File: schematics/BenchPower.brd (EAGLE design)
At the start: 79.7 x 67 mm, 28 parts, among them U1 V_REG_317SINK

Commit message: New layout
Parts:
- moved JP7 50.8 mm to (8.89, 6.99), turned to 90 degrees
- moved U$3 49.8 mm to (1.91, 58.7)
- moved JP2 46.4 mm to (51.4, 3.81), turned to 0 degrees
- moved JP6 26.7 mm to (31.8, 3.81), turned to 0 degrees
- moved R1 6.87 mm to (31.8, 31.8)
- moved LED1 3.18 mm to (33.0, 10.2)
- moved PWR1 3.18 mm to (62.9, 6.35)
- moved PWR2 3.18 mm to (23.5, 6.35)
- moved U$5 3.17 mm to (43.2, 6.35)
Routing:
- net 5VATX: track 55.1 -> 99.9 mm
- net AMPS12VHDR: track 68.8 -> 61.0 mm
- net 12VHDR: track 103.8 -> 96.6 mm
- net N$1: track 15.0 -> 17.8 mm
- net AMPS12VREG: track 66.1 -> 63.5 mm
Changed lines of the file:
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@@
 <wire x1="79.6825" y1="67" x2="0" y2="67" width="0" layer="20"/>
 <wire x1="0" y1="67" x2="0" y2="0" width="0" layer="20"/>
-<text x="1.27" y="10.795" size="1.27" layer="21" font="vector">cjd@chrisd.info</text>
-<text x="65.0875" y="10.795" size="1.27" layer="21" font="vector">v2.0 (c) 2015</text>
-<text x="64.135" y="1.27" size="1.27" layer="21" font="vector">adj</text>
-<text x="24.765" y="1.27" size="1.27" layer="21" font="vector">12v</text>
-<text x="43.18" y="12.7" size="1.27" layer="21" font="vector">blog.chrisd.info</text>
-<text x="45.085" y="1.27" size="1.27" layer="21" font="vector">gnd</text>
-<text x="6.985" y="4.445" size="1.27" layer="21" font="vector">12v</text>
-<text x="6.985" y="1.905" size="1.27" layer="21" font="vector">gnd</text>
+<text x="1.905" y="53.975" size="1.27" layer="21" font="vector">cjd@chrisd.info</text>
+<text x="1.905" y="56.515" size="1.27" layer="21" font="vector">v2.0 (c) 2015</text>
+<text x="27.94" y="1.27" size="1.27" layer="21" font="vector">12v</text>
+<text x="1.905" y="51.435" size="1.27" layer="21" font="vector">blog.chrisd.info</text>
+<text x="48.26" y="1.27" size="1.27" layer="21" font="vector">gnd</text>
 <text x="73.025" y="5.715" size="1.27" layer="21" font="vector" rot="R180">adj</text>
 <text x="73.025" y="3.175" size="1.27" layer="21" font="vector" rot="R180">gnd</text>
@@
 </autorouter>
 <elements>
-<element name="PWR1" library="desjardins" package="BINDINGPOST" value="BINDINGPOST" x="59.69" y="6.35"/>
-<element name="PWR2" library="desjardins" package="BINDINGPOST" value="BINDINGPOST" x="20.32" y="6.35"/>
-<element name="U$5" library="desjardins" package="BINDINGPOST" value="BINDINGPOST" x="40.005" y="6.35"/>
+<element name="PWR1" library="desjardins" package="BINDINGPOST" value="BINDINGPOST" x="62.865" y="6.35"/>
+<element name="PWR2" library="desjardins" package="BINDINGPOST" value="BINDINGPOST" x="23.495" y="6.35"/>
+<element name="U$5" library="desjardins" package="BINDINGPOST" value="BINDINGPOST" x="43.18" y="6.35"/>
 <element name="ATXCONN" library="desjardins" package="ATXPOWER" value="ATXPOWER" x="48.26" y="55.88" rot="R270"/>
 <element name="ARDUINOMICRO" library="ChrisD" package="ARDUINO_PRO_MICRO" value="ARDUINO_PRO_MICRO" x="78.105" y="22.225" rot="R90"/>
 <element name="U1" library="SparkFun-PowerIC" package="TO220-ADJ" value="V_REG_317SINK" x="77.47" y="61.595" rot="R270"/>
-<element name="R1" library="SparkFun-Passives" package="AXIAL-0.3" value="1000" x="26.035" y="27.94" rot="R270"/>
+<element name="R1" library="SparkFun-Passives" package="AXIAL-0.3" value="1000" x="31.75" y="31.75" rot="R270"/>
 <element name="R2" library="SparkFun-Passives" package="AXIAL-0.3" value="240" x="73.025" y="60.325" rot="R270"/>
-<element name="U$3" library="desjardins" package="LOGO" value="" x="21.59" y="13.0175"/>
+<element name="U$3" library="desjardins" package="LOGO" value="" x="1.905" y="58.7375"/>
 <element name="LCD" library="desjardins" package="DT162C" value="16X2LCDDT162C" x="40.01" y="31.135"/>
-<element name="LED1" library="adafruit" package="LED3MM" value="" x="29.845" y="10.16"/>
+<element name="LED1" library="adafruit" package="LED3MM" value="" x="33.02" y="10.16"/>
 <element name="R6" library="SparkFun-Resistors" package="1206" value="" x="48.895" y="32.385" rot="R180"/>
 <element name="R7" library="SparkFun-Resistors" package="1206" value="" x="65.405" y="32.385" rot="R180"/>
@@
 <element name="R8" library="SparkFun-Passives" package="AXIAL-0.3" value="gain" x="52.705" y="31.115" rot="R270"/>
 <element name="R9" library="SparkFun-Passives" package="AXIAL-0.3" value="gain" x="69.215" y="31.115" rot="R270"/>
-<element name="JP2" library="SparkFun-Connectors" package="1X02" value="M02PTH" x="5.08" y="2.54" rot="R180"/>
+<element name="JP2" library="SparkFun-Connectors" package="1X02" value="M02PTH" x="51.435" y="3.81"/>
 <element name="R3" library="SparkFun-Passives" package="AXIAL-0.3" value="100" x="55.245" y="31.115" rot="R90"/>
 <element name="R10" library="SparkFun-Passives" package="AXIAL-0.3" value="140" x="57.785" y="31.115" rot="R90"/>
 <element name="JP4" library="SparkFun-Connectors" package="1X02" value="M02PTH" x="74.93" y="2.54"/>
 <element name="JP5" library="SparkFun-Connectors" package="1X02" value="M02PTH" x="74.93" y="5.08"/>
-<element name="JP6" library="SparkFun-Connectors" package="1X02" value="M02PTH" x="5.08" y="5.08" rot="R180"/>
-<element name="JP7" library="SparkFun-Connectors" package="USB-A-S" value="USB-A-S" x="9.525" y="57.785"/>
+<element name="JP6" library="SparkFun-Connectors" package="1X02" value="M02PTH" x="31.75" y="3.81"/>
+<element name="JP7" library="SparkFun-Connectors" package="USB-A-S" value="USB-A-S" x="8.89" y="6.985" rot="R90"/>
 <element name="JP8" library="SparkFun-Connectors" package="1X03" value="" x="62.23" y="44.45"/>
 </elements>
@@
 <wire x1="40.005" y1="36.83" x2="57.785" y2="36.83" width="0.8128" layer="1"/>
 <wire x1="57.785" y1="36.83" x2="57.785" y2="34.925" width="0.8128" layer="1"/>
-<wire x1="31.115" y1="36.83" x2="36.83" y2="36.83" width="0.4064" layer="1"/>
-<wire x1="36.83" y1="36.83" x2="38.735" y2="38.735" width="0.4064" layer="1"/>
-<wire x1="31.115" y1="36.83" x2="26.035" y2="31.75" width="0.4064" layer="1"/>
+<wire x1="31.75" y1="35.56" x2="35.56" y2="35.56" width="0.4064" layer="1"/>
+<wire x1="35.56" y1="35.56" x2="38.735" y2="38.735" width="0.4064" layer="1"/>
 </signal>
 <signal name="N$1">
 <contactref element="R1" pad="P$2"/>
 <contactref element="LED1" pad="A"/>
-<wire x1="26.035" y1="24.13" x2="26.035" y2="12.7" width="0.4064" layer="16"/>
-<wire x1="26.035" y1="12.7" x2="28.575" y2="10.16" width="0.4064" layer="16"/>
+<wire x1="31.75" y1="27.94" x2="31.75" y2="10.16" width="0.4064" layer="1"/>
 </signal>
 <signal name="PWR_OK">
@@
 <wire x1="60.96" y1="26.67" x2="62.23" y2="25.4" width="0.8128" layer="1"/>
 <wire x1="62.23" y1="25.4" x2="74.93" y2="25.4" width="0.8128" layer="1"/>
-<wire x1="76.2" y1="22.225" x2="74.93" y2="20.955" width="0.8128" layer="1"/>
+<wire x1="76.2" y1="22.225" x2="74.295" y2="20.32" width="0.8128" layer="1"/>
 <wire x1="74.93" y1="5.08" x2="77.47" y2="5.08" width="0.8128" layer="16"/>
-<wire x1="74.93" y1="20.955" x2="74.93" y2="13.335" width="0.8128" layer="1"/>
-<wire x1="74.93" y1="13.335" x2="77.47" y2="10.795" width="0.8128" layer="1"/>
+<wire x1="74.295" y1="20.32" x2="74.295" y2="13.97" width="0.8128" layer="1"/>
+<wire x1="74.295" y1="13.97" x2="77.47" y2="10.795" width="0.8128" layer="1"/>
 <wire x1="77.47" y1="10.795" x2="77.47" y2="5.08" width="0.8128" layer="1"/>
-<wire x1="74.93" y1="5.08" x2="60.96" y2="5.08" width="0.8128" layer="16"/>
-<wire x1="60.96" y1="5.08" x2="59.69" y2="6.35" width="0.8128" layer="16"/>
+<wire x1="74.93" y1="5.08" x2="64.135" y2="5.08" width="0.8128" layer="16"/>
+<wire x1="64.135" y1="5.08" x2="62.865" y2="6.35" width="0.8128" layer="16"/>
 </signal>
 <signal name="AMPS12VHDR">
@@
 <wire x1="47.5949" y1="29.525" x2="47.5949" y2="31.6501" width="0.4064" layer="1"/>
 <wire x1="47.5949" y1="31.6501" x2="47.495" y2="32.385" width="0.6096" layer="1"/>
-<wire x1="20.32" y1="22.86" x2="20.32" y2="6.35" width="0.8128" layer="1"/>
-<wire x1="20.32" y1="22.86" x2="29.845" y2="32.385" width="0.8128" layer="1"/>
 <wire x1="29.845" y1="32.385" x2="47.495" y2="32.385" width="0.8128" layer="1"/>
 <contactref element="JP6" pad="2"/>
 <contactref element="JP6" pad="1"/>
-<wire x1="2.54" y1="5.08" x2="5.08" y2="5.08" width="0.8128" layer="16"/>
-<wire x1="5.08" y1="5.08" x2="19.05" y2="5.08" width="0.8128" layer="16"/>
-<wire x1="19.05" y1="5.08" x2="20.32" y2="6.35" width="0.8128" layer="16"/>
+<wire x1="29.845" y1="32.385" x2="23.495" y2="26.035" width="0.8128" layer="1"/>
+<wire x1="23.495" y1="26.035" x2="23.495" y2="6.35" width="0.8128" layer="1"/>
+<wire x1="23.495" y1="6.35" x2="29.21" y2="6.35" width="0.8128" layer="1"/>
+<wire x1="29.21" y1="6.35" x2="31.75" y2="3.81" width="0.8128" layer="1"/>
+<wire x1="31.75" y1="3.81" x2="34.29" y2="3.81" width="0.8128" layer="1"/>
 </signal>
 <signal name="3.3V$2">
@@
 <contactref element="LCD" pad="P$4"/>
 <contactref element="ARDUINOMICRO" pad="P3"/>
-<wire x1="35.56" y1="26.67" x2="38.735" y2="23.495" width="0.4064" layer="16"/>
-<wire x1="35.56" y1="26.67" x2="34.925" y2="26.67" width="0.4064" layer="16"/>
-<wire x1="34.925" y1="26.67" x2="15.875" y2="45.72" width="0.4064" layer="16"/>
-<wire x1="15.875" y1="45.72" x2="15.875" y2="46.89" width="0.4064" layer="16"/>
-<wire x1="15.875" y1="46.89" x2="15.63" y2="47.135" width="0.4064" layer="16"/>
+<wire x1="38.735" y1="23.495" x2="15.63" y2="46.6" width="0.4064" layer="16"/>
+<wire x1="15.63" y1="46.6" x2="15.63" y2="47.135" width="0.4064" layer="16"/>
 </signal>
 <signal name="LCD_EN">
@@
 <wire x1="62.865" y1="51.435" x2="62.865" y2="50.475" width="0.4064" layer="1"/>
 <wire x1="62.865" y1="50.475" x2="62.96" y2="50.38" width="0.4064" layer="1"/>
-<wire x1="60.96" y1="53.34" x2="22.86" y2="53.34" width="0.4064" layer="1"/>
-<wire x1="22.86" y1="53.34" x2="15.24" y2="60.96" width="0.4064" layer="1"/>
-<wire x1="15.24" y1="60.96" x2="13.15" y2="60.96" width="0.4064" layer="1"/>
-<wire x1="13.15" y1="60.96" x2="12.975" y2="60.785" width="0.4064" layer="1"/>
+<wire x1="60.96" y1="53.34" x2="9.525" y2="53.34" width="0.4064" layer="1"/>
+<wire x1="9.525" y1="53.34" x2="5.715" y2="49.53" width="0.4064" layer="1"/>
+<wire x1="5.715" y1="49.53" x2="5.715" y2="10.61" width="0.4064" layer="1"/>
+<wire x1="5.715" y1="10.61" x2="5.89" y2="10.435" width="0.4064" layer="1"/>
 </signal>
 <signal name="5V$4">

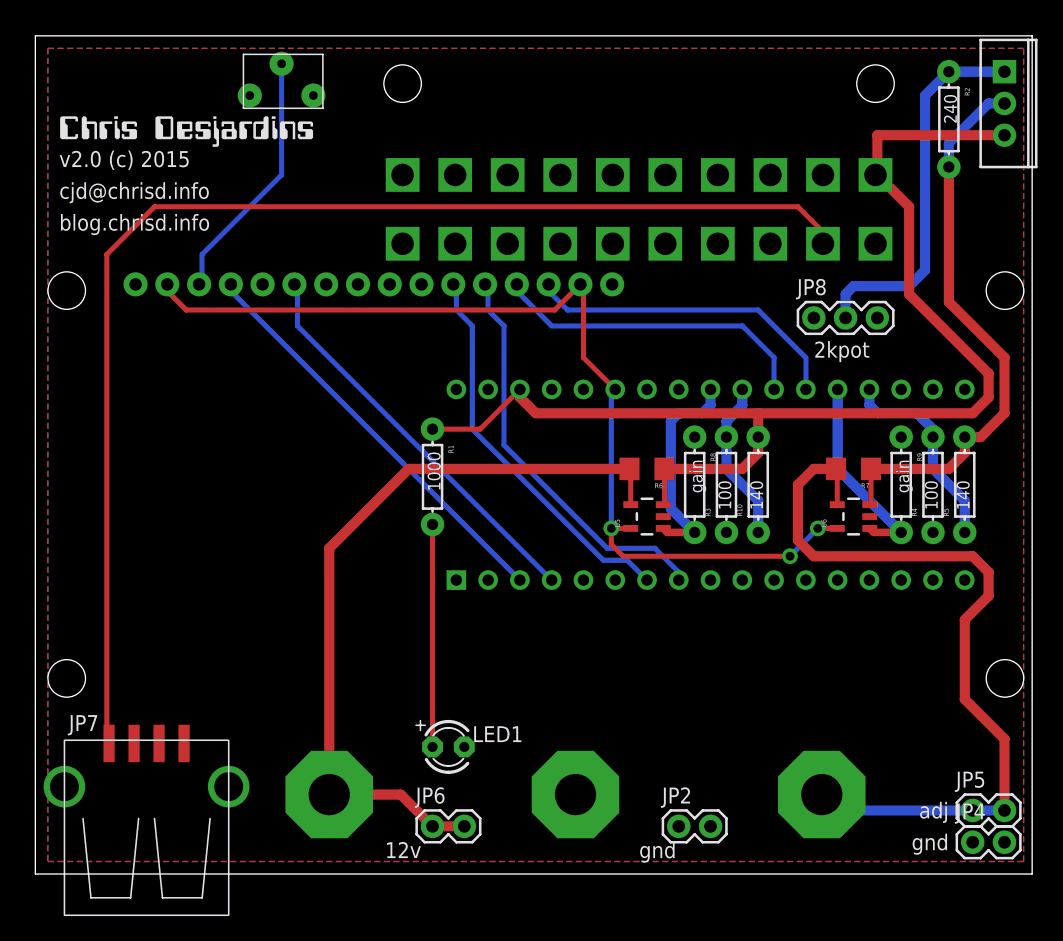
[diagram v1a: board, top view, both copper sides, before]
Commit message: Rearrange graphics
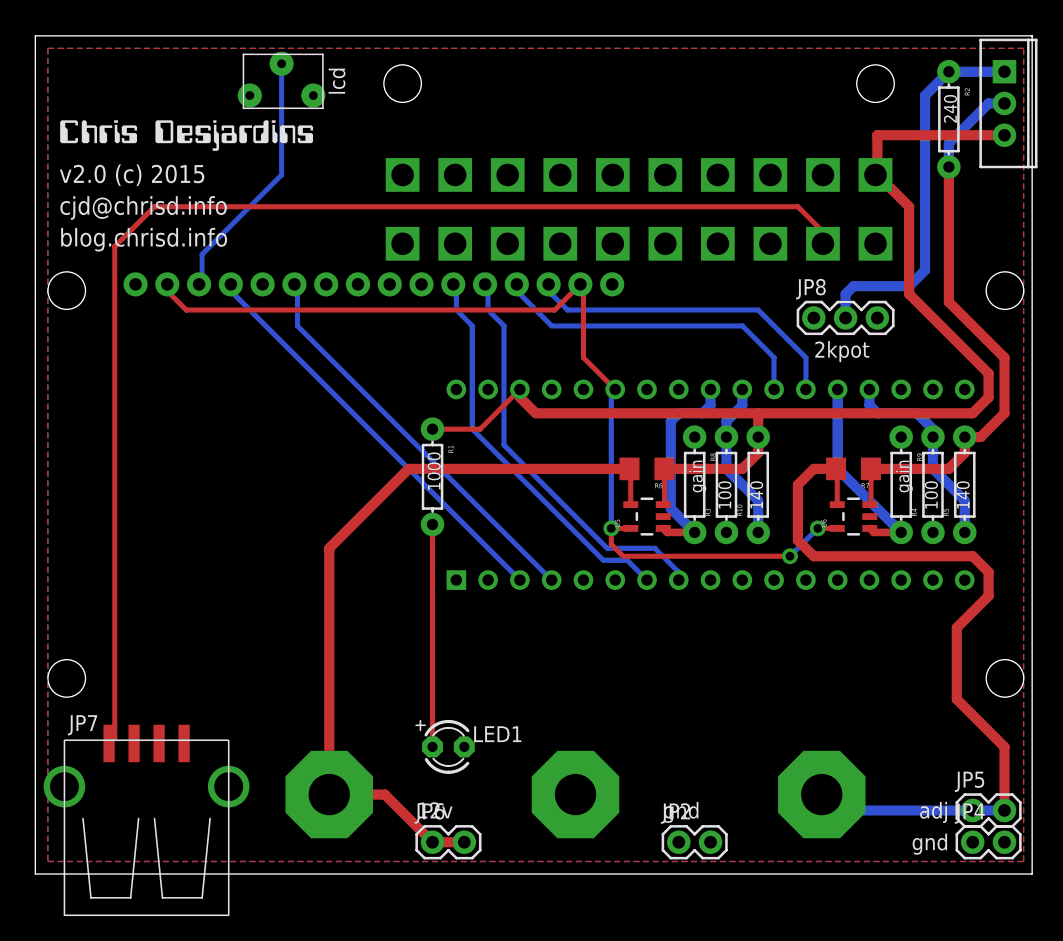
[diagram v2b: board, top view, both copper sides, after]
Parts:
- moved JP2 1.27 mm to (51.4, 2.54)
- moved JP6 1.27 mm to (31.8, 2.54)
- moved U$3 0.32 mm to (1.91, 58.4)
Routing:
- net AMPS12VHDR: track 61.0 -> 61.6 mm
- net AMPS12VREG: track 63.5 -> 64.0 mm
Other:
- board text added: "lcd"
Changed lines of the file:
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@@
 <wire x1="79.6825" y1="67" x2="0" y2="67" width="0" layer="20"/>
 <wire x1="0" y1="67" x2="0" y2="0" width="0" layer="20"/>
-<text x="1.905" y="53.975" size="1.27" layer="21" font="vector">cjd@chrisd.info</text>
-<text x="1.905" y="56.515" size="1.27" layer="21" font="vector">v2.0 (c) 2015</text>
-<text x="27.94" y="1.27" size="1.27" layer="21" font="vector">12v</text>
-<text x="1.905" y="51.435" size="1.27" layer="21" font="vector">blog.chrisd.info</text>
-<text x="48.26" y="1.27" size="1.27" layer="21" font="vector">gnd</text>
+<text x="1.905" y="52.705" size="1.4224" layer="21" font="vector">cjd@chrisd.info</text>
+<text x="1.905" y="55.245" size="1.4224" layer="21" font="vector">v2.0 (c) 2015</text>
+<text x="30.48" y="4.445" size="1.27" layer="21" font="vector">12v</text>
+<text x="1.905" y="50.165" size="1.4224" layer="21" font="vector">blog.chrisd.info</text>
+<text x="50.165" y="4.445" size="1.27" layer="21" font="vector">gnd</text>
 <text x="73.025" y="5.715" size="1.27" layer="21" font="vector" rot="R180">adj</text>
 <text x="73.025" y="3.175" size="1.27" layer="21" font="vector" rot="R180">gnd</text>
 <text x="62.23" y="41.275" size="1.27" layer="21" font="vector">2kpot</text>
+<text x="24.765" y="62.23" size="1.27" layer="21" font="vector" rot="R90">lcd</text>
 </plain>
 <attributes>
@@
 <element name="R1" library="SparkFun-Passives" package="AXIAL-0.3" value="1000" x="31.75" y="31.75" rot="R270"/>
 <element name="R2" library="SparkFun-Passives" package="AXIAL-0.3" value="240" x="73.025" y="60.325" rot="R270"/>
-<element name="U$3" library="desjardins" package="LOGO" value="" x="1.905" y="58.7375"/>
+<element name="U$3" library="desjardins" package="LOGO" value="" x="1.905" y="58.42"/>
 <element name="LCD" library="desjardins" package="DT162C" value="16X2LCDDT162C" x="40.01" y="31.135"/>
 <element name="LED1" library="adafruit" package="LED3MM" value="" x="33.02" y="10.16"/>
@@
 <element name="R8" library="SparkFun-Passives" package="AXIAL-0.3" value="gain" x="52.705" y="31.115" rot="R270"/>
 <element name="R9" library="SparkFun-Passives" package="AXIAL-0.3" value="gain" x="69.215" y="31.115" rot="R270"/>
-<element name="JP2" library="SparkFun-Connectors" package="1X02" value="M02PTH" x="51.435" y="3.81"/>
+<element name="JP2" library="SparkFun-Connectors" package="1X02" value="M02PTH" x="51.435" y="2.54"/>
 <element name="R3" library="SparkFun-Passives" package="AXIAL-0.3" value="100" x="55.245" y="31.115" rot="R90"/>
 <element name="R10" library="SparkFun-Passives" package="AXIAL-0.3" value="140" x="57.785" y="31.115" rot="R90"/>
 <element name="JP4" library="SparkFun-Connectors" package="1X02" value="M02PTH" x="74.93" y="2.54"/>
 <element name="JP5" library="SparkFun-Connectors" package="1X02" value="M02PTH" x="74.93" y="5.08"/>
-<element name="JP6" library="SparkFun-Connectors" package="1X02" value="M02PTH" x="31.75" y="3.81"/>
+<element name="JP6" library="SparkFun-Connectors" package="1X02" value="M02PTH" x="31.75" y="2.54"/>
 <element name="JP7" library="SparkFun-Connectors" package="USB-A-S" value="USB-A-S" x="8.89" y="6.985" rot="R90"/>
 <element name="JP8" library="SparkFun-Connectors" package="1X03" value="" x="62.23" y="44.45"/>
@@
 <wire x1="60.96" y1="26.67" x2="62.23" y2="25.4" width="0.8128" layer="1"/>
 <wire x1="62.23" y1="25.4" x2="74.93" y2="25.4" width="0.8128" layer="1"/>
-<wire x1="76.2" y1="22.225" x2="74.295" y2="20.32" width="0.8128" layer="1"/>
+<wire x1="76.2" y1="22.225" x2="73.66" y2="19.685" width="0.8128" layer="1"/>
 <wire x1="74.93" y1="5.08" x2="77.47" y2="5.08" width="0.8128" layer="16"/>
-<wire x1="74.295" y1="20.32" x2="74.295" y2="13.97" width="0.8128" layer="1"/>
-<wire x1="74.295" y1="13.97" x2="77.47" y2="10.795" width="0.8128" layer="1"/>
-<wire x1="77.47" y1="10.795" x2="77.47" y2="5.08" width="0.8128" layer="1"/>
+<wire x1="73.66" y1="19.685" x2="73.66" y2="13.97" width="0.8128" layer="1"/>
+<wire x1="73.66" y1="13.97" x2="77.47" y2="10.16" width="0.8128" layer="1"/>
+<wire x1="77.47" y1="10.16" x2="77.47" y2="5.08" width="0.8128" layer="1"/>
 <wire x1="74.93" y1="5.08" x2="64.135" y2="5.08" width="0.8128" layer="16"/>
 <wire x1="64.135" y1="5.08" x2="62.865" y2="6.35" width="0.8128" layer="16"/>
@@
 <wire x1="29.845" y1="32.385" x2="23.495" y2="26.035" width="0.8128" layer="1"/>
 <wire x1="23.495" y1="26.035" x2="23.495" y2="6.35" width="0.8128" layer="1"/>
-<wire x1="23.495" y1="6.35" x2="29.21" y2="6.35" width="0.8128" layer="1"/>
-<wire x1="29.21" y1="6.35" x2="31.75" y2="3.81" width="0.8128" layer="1"/>
-<wire x1="31.75" y1="3.81" x2="34.29" y2="3.81" width="0.8128" layer="1"/>
+<wire x1="31.75" y1="2.54" x2="34.29" y2="2.54" width="0.8128" layer="1"/>
+<wire x1="23.495" y1="6.35" x2="27.94" y2="6.35" width="0.8128" layer="1"/>
+<wire x1="27.94" y1="6.35" x2="31.75" y2="2.54" width="0.8128" layer="1"/>
 </signal>
 <signal name="3.3V$2">
@@
 <wire x1="62.865" y1="50.475" x2="62.96" y2="50.38" width="0.4064" layer="1"/>
 <wire x1="60.96" y1="53.34" x2="9.525" y2="53.34" width="0.4064" layer="1"/>
-<wire x1="9.525" y1="53.34" x2="5.715" y2="49.53" width="0.4064" layer="1"/>
-<wire x1="5.715" y1="49.53" x2="5.715" y2="10.61" width="0.4064" layer="1"/>
 <wire x1="5.715" y1="10.61" x2="5.89" y2="10.435" width="0.4064" layer="1"/>
+<wire x1="9.525" y1="53.34" x2="6.35" y2="50.165" width="0.4064" layer="1"/>
+<wire x1="6.35" y1="50.165" x2="6.35" y2="10.895" width="0.4064" layer="1"/>
+<wire x1="6.35" y1="10.895" x2="5.89" y2="10.435" width="0.4064" layer="1"/>
 </signal>
 <signal name="5V$4">

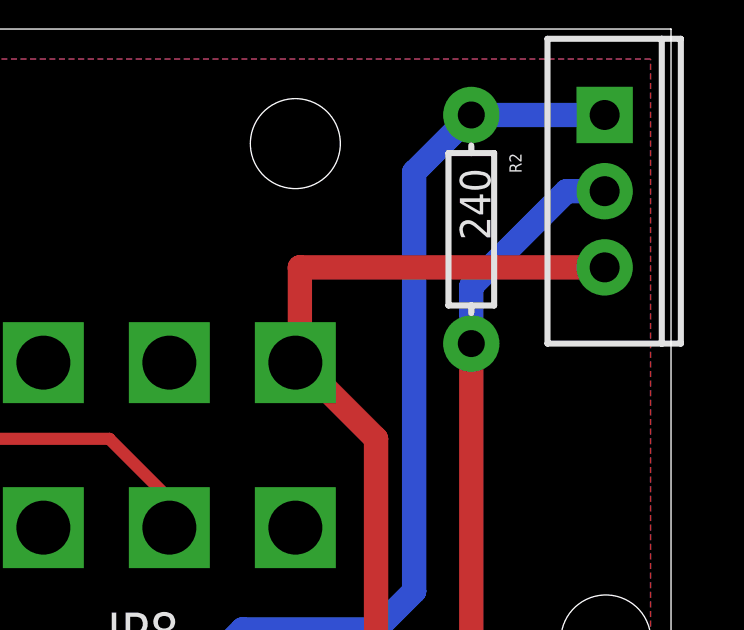
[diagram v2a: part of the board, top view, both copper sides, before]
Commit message: Reroute a line
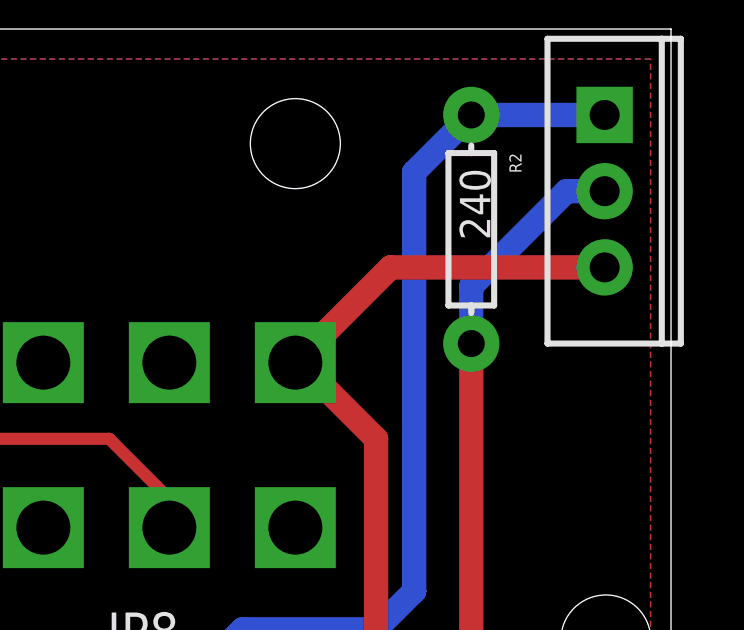
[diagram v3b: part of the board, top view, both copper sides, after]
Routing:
- net 12VHDR: track 96.6 -> 94.8 mm
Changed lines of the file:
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@@
 <wire x1="57.785" y1="33.655" x2="56.515" y2="32.385" width="0.8128" layer="1"/>
 <wire x1="56.515" y1="32.385" x2="50.295" y2="32.385" width="0.8128" layer="1"/>
-<wire x1="67.31" y1="59.055" x2="77.47" y2="59.055" width="0.8128" layer="1"/>
-<wire x1="67.31" y1="59.055" x2="67.31" y2="56.03" width="0.8128" layer="1"/>
-<wire x1="67.31" y1="56.03" x2="67.16" y2="55.88" width="0.8128" layer="1"/>
 <wire x1="40.005" y1="36.83" x2="57.785" y2="36.83" width="0.8128" layer="1"/>
 <wire x1="57.785" y1="36.83" x2="57.785" y2="34.925" width="0.8128" layer="1"/>
 <wire x1="31.75" y1="35.56" x2="35.56" y2="35.56" width="0.4064" layer="1"/>
 <wire x1="35.56" y1="35.56" x2="38.735" y2="38.735" width="0.4064" layer="1"/>
+<wire x1="77.47" y1="59.055" x2="70.335" y2="59.055" width="0.8128" layer="1"/>
+<wire x1="70.335" y1="59.055" x2="67.16" y2="55.88" width="0.8128" layer="1"/>
 </signal>
 <signal name="N$1">
